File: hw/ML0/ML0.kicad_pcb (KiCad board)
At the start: 2 copper layers, 59 parts, among them J1 Rig Connector, J2 12V Supply, J3 Digital Connector, J4 ADC Connector, U1 LMV321, U2 LTV-356T, U3 NCP1117-3.3_SOT223, U4 MCP4725xxx-xCH, U5 LTV-356T, U9 LMV324

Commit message: Initial layout done
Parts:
- added J5: Conn_01x03, Connector_PinHeader_2.54mm:PinHeader_1x03_P2.54mm_Vertical, F.Cu at (151.0, 71.1)
- added R19: 1k, Resistor_SMD:R_0805_2012Metric_Pad1.20x1.40mm_HandSolder, F.Cu at (216.5, 85.0)
- added R20: 570, Resistor_SMD:R_0805_2012Metric_Pad1.20x1.40mm_HandSolder, F.Cu at (238.0, 102.0)
- added T1: Transformer_1P_1S, KiCad-Library:CheapAudioTransformer, F.Cu at (228.0, 95.0)
- added T2: Transformer_1P_1S, KiCad-Library:CheapAudioTransformer, F.Cu at (228.2, 63.0)
- C1, C20: value 470u -> 100u; footprint Capacitor_SMD:CP_Elec_8x10 -> KiCad-Library:CAP_KEMET_530_530
- C10: value 10u (Optional DC Block) -> 47u (Optional DC Block)
- C19, C24, C7, C8, C9: footprint Capacitor_SMD:CP_Elec_8x10 -> KiCad-Library:CAP_KEMET_530_530
- C6: value 4.7u -> 100u; footprint Capacitor_SMD:CP_Elec_8x10 -> KiCad-Library:CAP_KEMET_530_530
- J1: value Rig Connector -> Conn_01x06; footprint Connector_PinHeader_2.54mm:PinHeader_1x07_P2.54mm_Vertical -> Connector_PinHeader_2.54mm:PinHeader_1x06_P2.54mm_Vertical
- J4: footprint Connector_Wire:SolderWire-2.5sqmm_1x02_P7.2mm_D2.4mm_OD3.6mm_Relief -> Connector_PinHeader_2.54mm:PinHeader_1x02_P2.54mm_Vertical
- R3: value 10k -> 1k
- moved H1 114.9 mm to (252.0, 101.0)
- moved H2 107.7 mm to (252.0, 53.0)
- moved J1 98.8 mm to (251.0, 62.6)
- moved C10 85.1 mm to (247.0, 81.0), turned to -90 degrees
- moved R3 70.1 mm to (241.0, 102.0), turned to -90 degrees
- moved R8 65.6 mm to (236.0, 76.0), turned to 180 degrees
- moved U2 63.9 mm to (229.0, 81.0)
- moved RV1 63.8 mm to (245.0, 91.0), turned to 90 degrees
- moved U5 56.7 mm to (229.0, 75.0), turned to 180 degrees
- moved R4 54.1 mm to (220.0, 80.0)
- moved RV3 53.0 mm to (211.0, 71.8), turned to -90 degrees
- moved C6 49.3 mm to (208.8, 89.2), turned to 90 degrees
- moved C24 47.3 mm to (200.0, 56.4), turned to 90 degrees
- moved J4 47.1 mm to (168.0, 70.3)
- moved C9 41.7 mm to (184.6, 81.5), turned to 180 degrees
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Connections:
- C10 pad 1: RIG_AF_OUT -> RIG_AF_IN
- C10 pad 2: Net-(T1-SB) -> Net-(C10-Pad2)
- C17 pad 2: Net-(U9A-+) -> Net-(U9C-+)
- C18 pad 1: Net-(U9A-+) -> Net-(U9C-+)
- C22 pad 1: Net-(U9A--) -> Net-(U9C--)
- C22 pad 2: Net-(U9C-+) -> Net-(U9D-+)
- C29 pad 1: Net-(U9D--) -> Net-(U9A--)
- J1 pad 1: RIG_GND -> RIG_AF_OUT+
- J1 pad 2: RIG_AF_IN -> RIG_AF_OUT-
- J1 pad 3: RIG_GND -> RIG_COS
- J1 pad 4: RIG_AF_OUT -> RIG_GND
- J1 pad 5: RIG_GND -> RIG_PTT
- J1 pad 6: RIG_PTT -> RIG_AF_IN
- J3 pad 1: IC20_SDA -> GPIO_COS
- J3 pad 2: IC20_SCL -> GPIO_PTT
- J3 pad 3: GPIO_COS -> IC20_SDA
- J3 pad 4: GPIO_PTT -> IC20_SCL
- R10 pad 2: Net-(U9A-+) -> Net-(U9C-+)
- R11 pad 1: Net-(U9A-+) -> Net-(U9C-+)
- R12 pad 2: Net-(U9A--) -> Net-(U9C--)
- R13 pad 1: Net-(U9A--) -> Net-(U9C--)
- R13 pad 2: Net-(U9C-+) -> Net-(U9D-+)
- R14 pad 2: Net-(U9C--) -> Net-(U9D--)
- R15 pad 2: Net-(U9C-+) -> Net-(U9D-+)
- R16 pad 1: Net-(U9C--) -> Net-(U9D--)
- R16 pad 2: Net-(U9D-+) -> Net-(U9A-+)
- R3 pad 1: Net-(C6-Pad2) -> Net-(T1-SB)
- R9 pad 2: GPIO_COS -> Net-(J5-Pin_1)
- RV1 pad 2: Net-(T1-AA) -> Net-(C10-Pad2)
- RV1 pad 3: GNDA -> RIG_GND
- RV4 pad 2: Net-(U9D--) -> Net-(U9A--)
- U5 pad 4: GPIO_COS -> Net-(J5-Pin_1)
- U9 pad 1: Net-(U9C-+) -> Net-(J5-Pin_3)
- U9 pad 14: GPIO_COS -> Net-(U9A-+)
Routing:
- net GPIO_PTT: track 0.00 -> 82.0 mm
- net GNDA: track 0.00 -> 78.5 mm, vias 0 -> 26
- net Net-(J5-Pin_1): track 0.00 -> 78.3 mm
- net IC20_SDA: track 0.00 -> 50.3 mm
- net IC20_SCL: track 0.00 -> 49.5 mm
- net Net-(J5-Pin_3): track 0.00 -> 47.2 mm
- net +3.3VA: track 0.00 -> 39.5 mm, vias 0 -> 3
- net Net-(U9C-+): track 0.00 -> 32.9 mm
- net RIG_PTT: track 0.00 -> 21.7 mm
- net Net-(U1--): track 0.00 -> 18.8 mm
- net RIG_COS: track 0.00 -> 17.4 mm
- net Net-(U9D-+): track 0.00 -> 15.8 mm
- net RIG_AF_OUT+: track 0.00 -> 14.2 mm
- net Net-(U9B--): track 0.00 -> 13.9 mm
- net RIG_AF_OUT-: track 0.00 -> 13.4 mm
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- added copper zone on F.Cu, net +3.3VA
- added copper zone on B.Cu, net GNDA
- added copper zone on F.Cu, net RIG_GND
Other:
- board outline added: 120 x 60 mm

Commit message: Working on PCB
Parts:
- moved J2 15.3 mm to (153.7, 102.0), turned to 90 degrees
- moved R6 4.61 mm to (152.0, 84.5)
- moved J3 2.75 mm to (144.0, 67.1)
- moved H4 2.24 mm to (145.0, 101.0)
- moved H1 1.00 mm to (251.0, 101.0)
- moved H2 1.00 mm to (251.0, 53.0)
- moved H3 1.00 mm to (145.0, 53.0)
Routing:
- net +12V: track 12.4 -> 24.7 mm
- net IC20_SDA: track 50.3 -> 47.6 mm
- net GPIO_PTT: track 82.0 -> 79.3 mm
- net GPIO_COS: track 10.4 -> 7.60 mm
- net IC20_SCL: track 49.5 -> 48.5 mm
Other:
- board size 120 x 60 mm -> 116.5 x 60 mm
- board text added: "+"
- board text added: "+12V"
- board text added: "1"
- board text added: "ADC"
- board text added: "COS"
- board text added: "MicroLink V0 2024-02 KC1FSZ"
- board text added: "Rig"

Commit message: Improvements to board
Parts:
- moved R3 13.7 mm to (238.5, 88.5), turned to 90 degrees
- moved J5 12.7 mm to (163.5, 73.0)
- moved J2 12.3 mm to (155.0, 89.7), turned to 0 degrees
- moved J3 12.2 mm to (155.0, 72.4)
- moved C8 11.9 mm to (163.0, 99.0)
- moved H3 10.0 mm to (155.0, 53.5)
- moved H4 10.0 mm to (155.0, 101.0)
- moved R20 7.43 mm to (240.5, 95.0), turned to 0 degrees
- moved H2 6.52 mm to (244.5, 53.5)
- moved H1 6.50 mm to (244.5, 101.0)
- moved J1 6.50 mm to (244.5, 62.6)
- moved D1 6.17 mm to (176.0, 96.5)
- moved R7 6.17 mm to (176.0, 92.2)
- moved C20 5.50 mm to (162.5, 59.4)
- moved C7 5.34 mm to (170.0, 99.0)
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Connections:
- R20 pad 1: Net-(T1-SB) -> Net-(T1-SA)
- R3 pad 1: Net-(T1-SB) -> Net-(T1-SA)
- T1 pad 3: RIG_GND -> Net-(T1-SA)
- T1 pad 4: Net-(T1-SB) -> RIG_GND
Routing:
- net +3.3VA: track 39.5 -> 24.3 mm, vias 3 -> 4
- net GPIO_PTT: track 79.3 -> 66.1 mm
- net IC20_SCL: track 48.5 -> 36.6 mm
- net RIG_GND: track 0.00 -> 11.6 mm
- net Net-(J5-Pin_3): track 47.2 -> 35.8 mm
- net IC20_SDA: track 47.6 -> 37.8 mm
- net Net-(J5-Pin_1): track 78.3 -> 68.7 mm
- net Net-(R3-Pad2): track 11.7 -> 4.07 mm
- net Net-(T1-SA): track 0.00 -> 7.16 mm
- net Net-(T1-SB): track 6.67 -> 0.00 mm
- net RIG_AF_OUT-: track 13.4 -> 6.89 mm
- net RIG_AF_OUT+: track 14.2 -> 7.66 mm
- net RIG_PTT: track 21.7 -> 15.2 mm
- net RIG_COS: track 17.4 -> 11.4 mm
- net +12V: track 24.7 -> 19.6 mm
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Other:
- board size 116.5 x 60 mm -> 100 x 59 mm

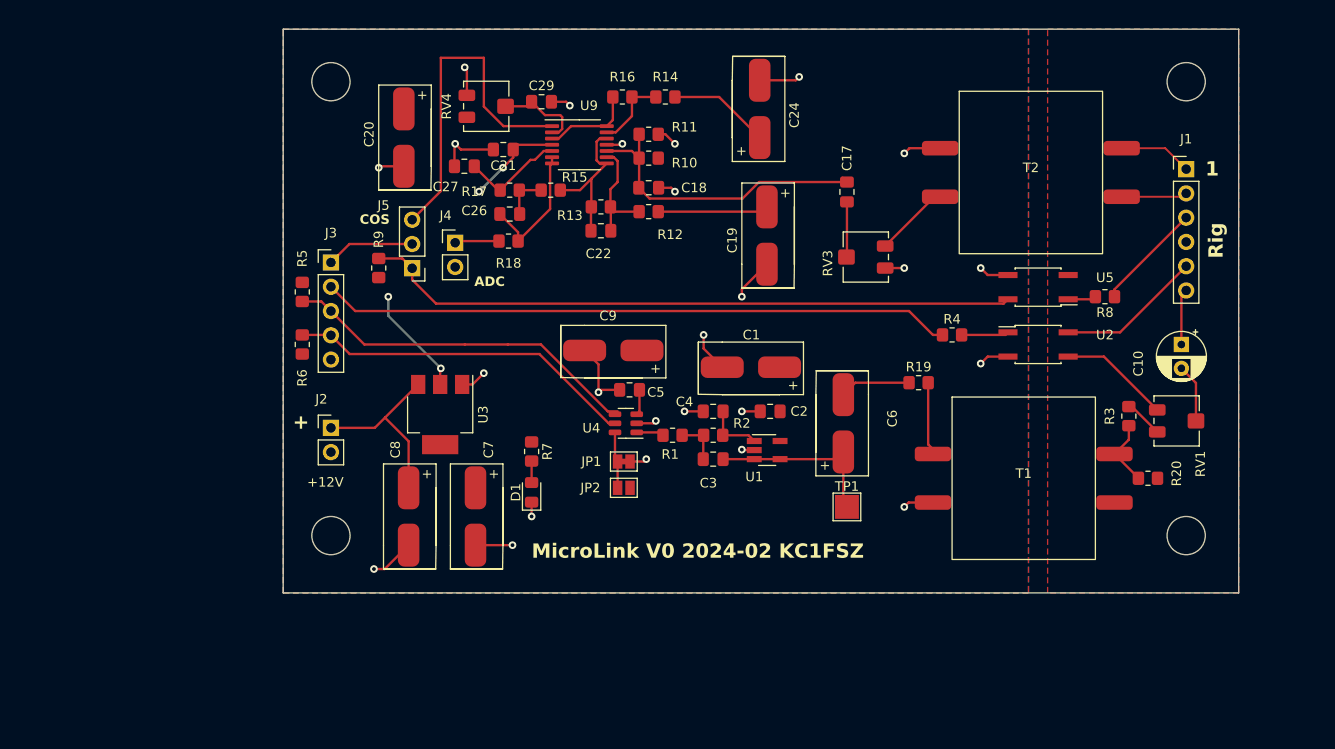
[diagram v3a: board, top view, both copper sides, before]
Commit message: Board sent to JLC on 2024-02-26 09:18 EST
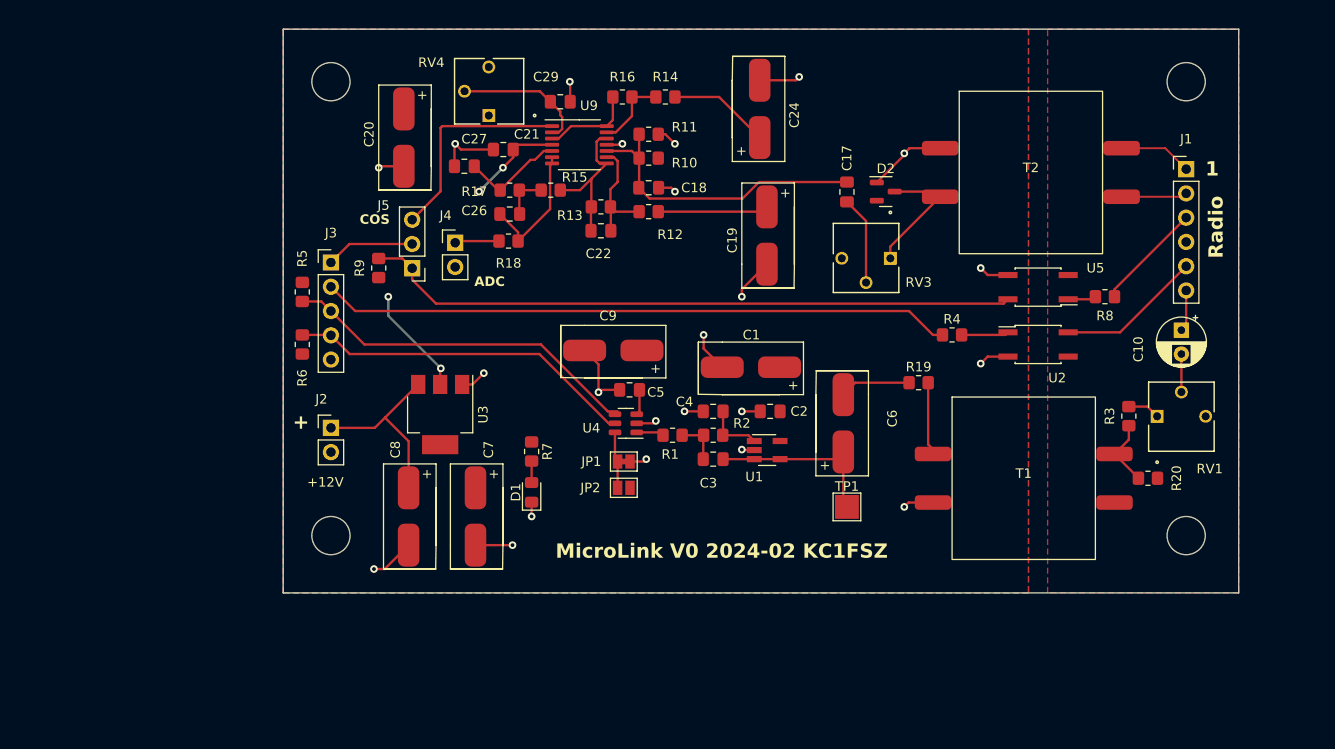
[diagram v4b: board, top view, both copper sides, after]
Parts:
- added D2: BAT54S, Package_TO_SOT_SMD:SOT-23, F.Cu at (213.1, 65.0)
- RV1, RV3, RV4: footprint Potentiometer_SMD:Potentiometer_Bourns_3314S_Horizontal -> KiCad-Library:POT_3362P
- moved RV3 2.57 mm to (213.5, 72.0), turned to 180 degrees
- moved RV1 2.10 mm to (241.5, 88.5), turned to 0 degrees
- moved C29 1.96 mm to (179.0, 55.6)
- moved C10 1.50 mm to (244.0, 79.5)
- moved RV4 1.00 mm to (171.5, 57.0)
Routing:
- net Net-(J5-Pin_3): track 35.8 -> 22.6 mm
- net RIG_GND: track 11.6 -> 0.00 mm
- net Net-(D2-COM): track 7.89 -> 13.6 mm
- net Net-(U9A--): track 9.24 -> 14.0 mm
- net Net-(C17-Pad1): track 5.80 -> 9.28 mm
- net Net-(C10-Pad2): track 6.13 -> 3.98 mm
- net RIG_AF_IN: track 5.86 -> 4.36 mm
- net GNDA: track 78.3 -> 77.5 mm, vias 25 -> 23
- net Net-(R3-Pad2): track 4.07 -> 3.38 mm
- net Net-(U9C-+): track 32.9 -> 32.3 mm
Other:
- board text added: "Radio"
- board text removed: "Rig"
